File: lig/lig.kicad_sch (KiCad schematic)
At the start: 58 parts, among them J1 In_Smart, J10 OutSmart, J11 Conn_01x01_Female, J12 Conn_01x01_Female, J13 Conn_01x01_Female, J14 Conn_01x01_Female, J15 Conn_01x02_Male, J16 Conn_01x02_Socket, J2 OutSmart, J3 In_Dumb, J4 Out_Dumb, J5 OutSmart, J6 OutSmart, J7 OutSmart, J8 OutSmart, J9 OutSmart, U1 AP63205WU, U3 WeMos_D1_mini

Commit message: added footprint
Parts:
- added C5: 100pf only for 63200, Capacitor_SMD:C_0603_1608Metric, symbol Device:C
- added D27: LevelShifter Diode, Diode_SMD:D_SOD-123F, symbol Device:D
- added D31: Level Shifter Diode, Diode_SMD:D_SOD-123F, symbol Device:D
- added J17, J18: Conn_01x03, Connector_PinHeader_2.54mm:PinHeader_1x03_P2.54mm_Vertical, symbol Connector_Generic:Conn_01x03
- added JP1, JP2: Close, Resistor_SMD:R_0603_1608Metric_Pad0.98x0.95mm_HandSolder, symbol Jumper:SolderJumper_2_Open
- added JP4: close if using 4.5V (ap63200) or using diode shif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, Resistor_SMD:R_0603_1608Metric_Pad0.98x0.95mm_HandSolder, symbol Jumper:SolderJumper_2_Open
- added JP5: close for 63205, Resistor_SMD:R_0603_1608Metric_Pad0.98x0.95mm_HandSolder, symbol Jumper:SolderJumper_2_Open
- added Q1: 2N7000, Package_TO_SOT_SMD:SOT-23, symbol Transistor_FET:2N7000
- added R10, R11, R4, R5, R8, R9: 10k, Resistor_SMD:R_0603_1608Metric, symbol Device:R
- added R6: 30k only for 63200, Resistor_SMD:R_0603_1608Metric, symbol Device:R
- added R7: 140k only for 63200, Resistor_SMD:R_0603_1608Metric, symbol Device:R
- added U2: LM393, Package_SO:SOIC-8_3.9x4.9mm_P1.27mm, symbol Comparator:LM393
- J11, J12, J13, J14: symbol Connector:Conn_01x01_Female -> Connector:Conn_01x01_Socket
- J15: symbol Connector:Conn_01x02_Male -> Connector:Conn_01x02_Pin
- U1: value AP63205WU -> AP63205WU or AP63200
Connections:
- net 5V: now also C5.2, D27.2 (A), J17.3 (Pin_3), J18.3 (Pin_3), JP1.2 (B), JP5.2 (B), R11.1, R5.1, R6.1, U2.8 (V+); no longer D1.1 (VDD), U1.1 (FB)
- net GND: now also J17.1 (Pin_1), J18.1 (Pin_1), R7.2, R9.2, U2.4 (V-)
- net LDumbOut: now also J18.2 (Pin_2)
- net LOut: now also JP4.2 (B), Q1.3 (D), R11.2, R5.2, U2.1; no longer ESP1.30 (IO09), U3.11 (D4)
- net at D1.4 (DIN), R1.2, R2.2: now also J17.2 (Pin_2)
- net 3V3: now reaches U3.8 (3V3)
- net 3V3: now also ESP1.18 (3.3V), Q1.2 (G), R4.1, R8.1
- new net: D1.1 (VDD), D31.1 (K), JP2.1 (A)
- new net: D27.1 (K), D31.2 (A), JP1.1 (A), JP2.2 (B)
- new net: C5.1, JP5.1 (A), R6.2, R7.1, U1.1 (FB)
- new net: R10.2, U2.2 (-)
- new net: R8.2, R9.1, U2.3 (+)
- new net LOut3V3: ESP1.30 (IO09), JP4.1 (A), Q1.1 (S), R10.1, R4.2, U3.11 (D4)
- no-connect marks 18 -> 54
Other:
- moved on the sheet: C3, C4, J16

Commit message: v2 changes
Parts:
- removed R2: 1k, Resistor_SMD:R_0603_1608Metric, symbol Device:R
- added D32: 1A 5uA@1kV, Diode_SMD:D_SOD-123F, symbol Device:D
- D27, D31: LCSC C64898 -> (none)
- JP1, JP2, JP4, JP5: footprint Resistor_SMD:R_0603_1608Metric_Pad0.98x0.95mm_HandSolder -> Jumper:SolderJumper-2_P1.3mm_Bridged_Pad1.0x1.5mm
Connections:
- net 5V: now also D32.1 (K); no longer C3.1, C4.1, C5.2, J16.2 (Pin_2), JP5.2 (B), L1.2, R6.1
- net LOut: now also D1.4 (DIN), J17.2 (Pin_2), R1.2
- new net: C3.1, C4.1, C5.2, D32.2 (A), J16.2 (Pin_2), JP5.2 (B), L1.2, R6.1
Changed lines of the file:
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@@
   (junction (at 203.835 156.21) (diameter 0) (color 0 0 0 0)
   )
+  (junction (at 156.21 167.005) (diameter 0) (color 0 0 0 0)
+  )
   (junction (at 175.26 86.995) (diameter 0) (color 0 0 0 0)
   )
@@
     (stroke (width 0) (type default))
   )
+  (wire (pts (xy 165.1 26.67) (xy 172.72 26.67))
+    (stroke (width 0) (type default))
+  )
   (wire (pts (xy 33.02 132.08) (xy 33.02 146.685))
     (stroke (width 0) (type default))
@@
     )
   )
-  (global_label "5V" (shape input) (at 156.21 167.005 0) (fields_autoplaced)
+  (global_label "5V" (shape input) (at 163.83 167.005 0) (fields_autoplaced)
     (effects (font (size 1.27 1.27)) (justify left))
-    (property "Intersheetrefs" "${INTERSHEET_REFS}" (at 160.9212 166.9256 0)
+    (property "Intersheetrefs" "${INTERSHEET_REFS}" (at 168.5412 166.9256 0)
       (effects (font (size 1.27 1.27)) (justify left) hide)
     )
@@
       (effects (font (size 1.27 1.27)))
     )
-    (property "Footprint" "Resistor_SMD:R_0603_1608Metric_Pad0.98x0.95mm_HandSolder" (at 192.405 16.51 0)
+    (property "Footprint" "Jumper:SolderJumper-2_P1.3mm_Bridged_Pad1.0x1.5mm" (at 192.405 16.51 0)
       (effects (font (size 1.27 1.27)) hide)
     )
@@
       (effects (font (size 1.27 1.27)) (justify right))
     )
-    (property "Footprint" "Resistor_SMD:R_0603_1608Metric_Pad0.98x0.95mm_HandSolder" (at 125.73 170.815 0)
+    (property "Footprint" "Jumper:SolderJumper-2_P1.3mm_Bridged_Pad1.0x1.5mm" (at 125.73 170.815 0)
       (effects (font (size 1.27 1.27)) hide)
     )
@@
       (effects (font (size 1.27 1.27)))
     )
-    (property "Footprint" "Resistor_SMD:R_0603_1608Metric_Pad0.98x0.95mm_HandSolder" (at 203.835 127 0)
+    (property "Footprint" "Jumper:SolderJumper-2_P1.3mm_Bridged_Pad1.0x1.5mm" (at 203.835 127 0)
       (effects (font (size 1.27 1.27)) hide)
     )
@@
       (effects (font (size 1.27 1.27)) hide)
     )
-    (property "LCSC" "C64898" (at 192.405 12.7 0)
+    (property "LCSC" "" (at 192.405 12.7 0)
       (effects (font (size 1.27 1.27)) hide)
     )
@@
       (effects (font (size 1.27 1.27)))
     )
-    (property "Footprint" "Resistor_SMD:R_0603_1608Metric_Pad0.98x0.95mm_HandSolder" (at 201.295 16.51 0)
+    (property "Footprint" "Jumper:SolderJumper-2_P1.3mm_Bridged_Pad1.0x1.5mm" (at 201.295 16.51 0)
       (effects (font (size 1.27 1.27)) hide)
     )
@@
     )
   )
-  (symbol (lib_id "Device:R") (at 168.91 26.67 90) (unit 1)
-    (in_bom yes) (on_board yes) (dnp no) (fields_autoplaced)
-    (property "Reference" "R2" (at 168.91 20.32 90)
-      (effects (font (size 1.27 1.27)))
-    )
-    (property "Value" "1k" (at 168.91 22.86 90)
-      (effects (font (size 1.27 1.27)))
-    )
-    (property "Footprint" "Resistor_SMD:R_0603_1608Metric" (at 168.91 28.448 90)
-      (effects (font (size 1.27 1.27)) hide)
-    )
-    (property "Datasheet" "~" (at 168.91 26.67 0)
-      (effects (font (size 1.27 1.27)) hide)
-    )
-    (property "LCSC" "C21190" (at 168.91 26.67 0)
-      (effects (font (size 1.27 1.27)) hide)
-    )
-    (pin "1")
-    (pin "2")
-    (instances
-      (project "lig"
-        (path "/03d6a00f-a8c8-4eb8-91ea-299864b30e8f"
-          (reference "R2") (unit 1)
-        )
-      )
-    )
-  )
   (symbol (lib_id "Device:C") (at 138.43 175.895 0) (unit 1)
     (in_bom yes) (on_board yes) (dnp no) (fields_autoplaced)
@@
       (effects (font (size 1.27 1.27)) hide)
     )
-    (property "LCSC" "C64898" (at 201.295 12.7 0)
+    (property "LCSC" "" (at 201.295 12.7 0)
       (effects (font (size 1.27 1.27)) hide)
     )
@@
         )
       )
+    )
+  )
+  (symbol (lib_id "Device:D") (at 160.02 167.005 180) (unit 1)
+    (in_bom yes) (on_board yes) (dnp no) (fields_autoplaced)
+    (property "Reference" "D32" (at 160.02 160.02 0)
+      (effects (font (size 1.27 1.27)))
+    )
+    (property "Value" "1A 5uA@1kV" (at 160.02 162.56 0)
+      (effects (font (size 1.27 1.27)))
+    )
+    (property "Footprint" "Diode_SMD:D_SOD-123F" (at 160.02 167.005 0)
+      (effects (font (size 1.27 1.27)) hide)
+    )
+    (property "Datasheet" "~" (at 160.02 167.005 0)
+      (effects (font (size 1.27 1.27)) hide)
+    )
+    (property "LCSC" "C64898" (at 160.02 167.005 0)
+      (effects (font (size 1.27 1.27)) hide)
+    )
+    (property "Sim.Device" "D" (at 160.02 167.005 0)
+      (effects (font (size 1.27 1.27)) hide)
+    )
+    (property "Sim.Pins" "1=K 2=A" (at 160.02 167.005 0)
+      (effects (font (size 1.27 1.27)) hide)
+    )
+    (pin "1")
+    (pin "2")
+    (instances
+      (project "lig"
+        (path "/03d6a00f-a8c8-4eb8-91ea-299864b30e8f"
+          (reference "D32") (unit 1)
+        )
+      )

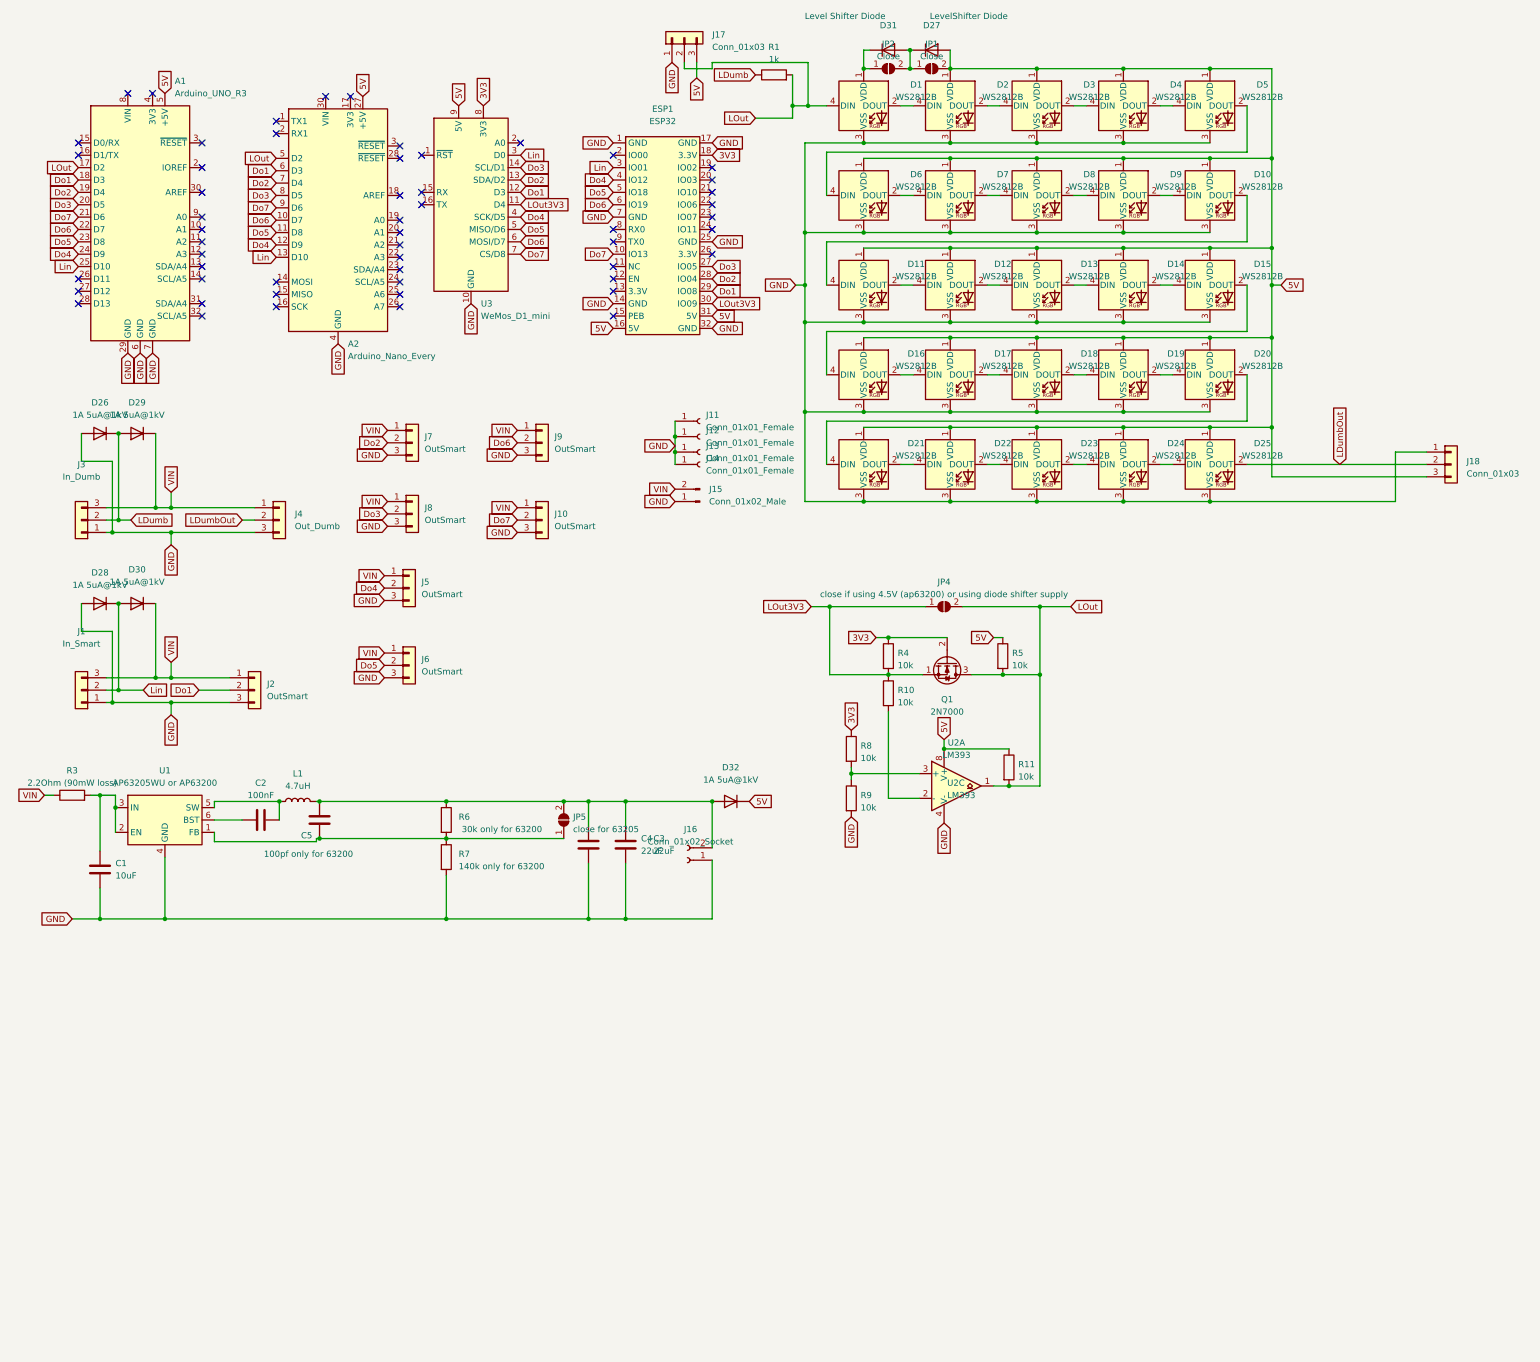
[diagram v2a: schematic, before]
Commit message: v2 diodes and simplification
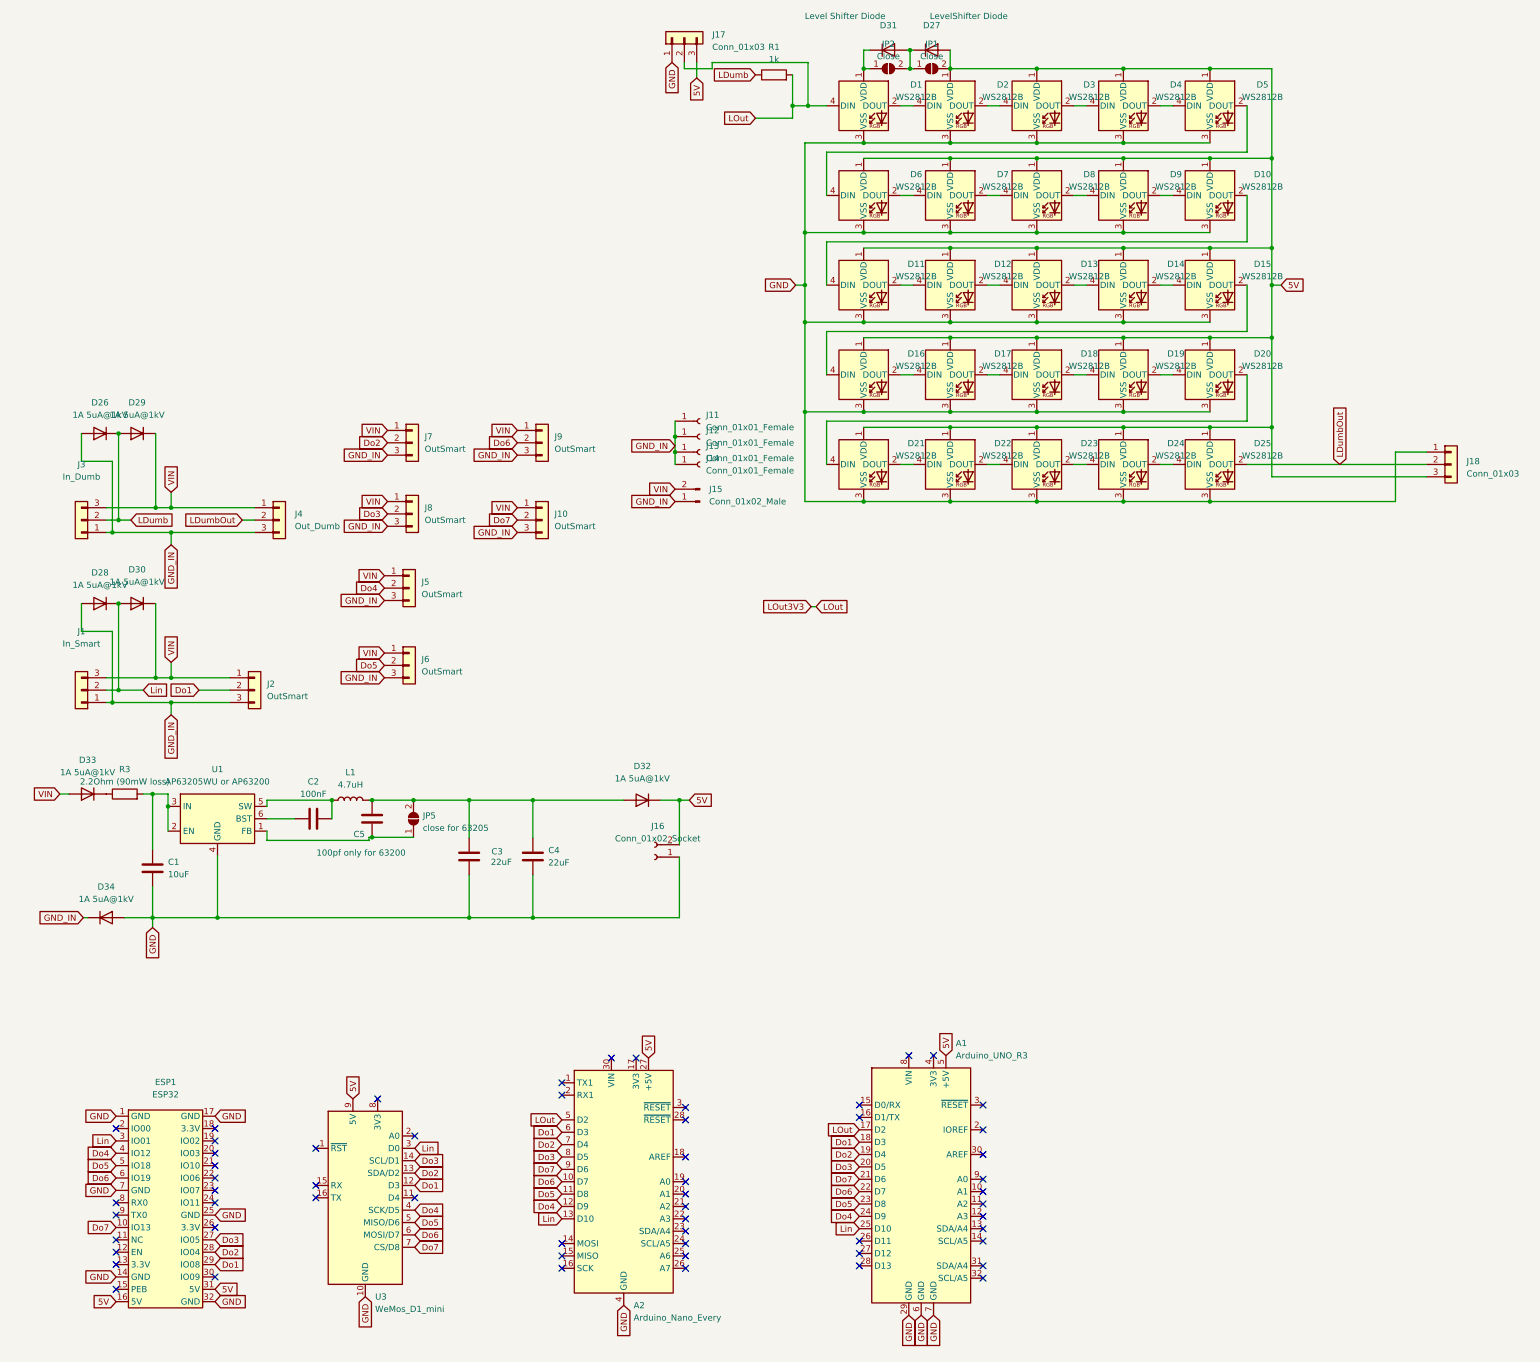
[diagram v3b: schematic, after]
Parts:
- removed JP4: close if using 4.5V (ap63200) or using diode shif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, Jumper:SolderJumper-2_P1.3mm_Bridged_Pad1.0x1.5mm, symbol Jumper:SolderJumper_2_Open
- removed Q1: 2N7000, Package_TO_SOT_SMD:SOT-23, symbol Transistor_FET:2N7000
- removed R10, R11, R4, R5, R8, R9: 10k, Resistor_SMD:R_0603_1608Metric, symbol Device:R
- removed R6: 30k only for 63200, Resistor_SMD:R_0603_1608Metric, symbol Device:R
- removed R7: 140k only for 63200, Resistor_SMD:R_0603_1608Metric, symbol Device:R
- removed U2: LM393, Package_SO:SOIC-8_3.9x4.9mm_P1.27mm, symbol Comparator:LM393
- added D33, D34: 1A 5uA@1kV, Diode_SMD:D_SOD-123F, symbol Device:D
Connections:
- net 5V: now also J16.2 (Pin_2)
- net GND: now also D34.2 (A); no longer D26.2 (A), D28.2 (A), J1.1 (Pin_1), J10.3 (Pin_3), J11.1 (Pin_1), J12.1 (Pin_1), J13.1 (Pin_1), J14.1 (Pin_1), J15.1 (Pin_1), J2.3 (Pin_3), J3.1 (Pin_1), J4.3 (Pin_3), J5.3 (Pin_3), J6.3 (Pin_3), J7.3 (Pin_3), J8.3 (Pin_3), J9.3 (Pin_3)
- net VIN: now also D33.2 (A); no longer R3.1
- net at C3.1, C4.1, C5.2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: no longer J16.2 (Pin_2)
- net 3V3: no longer names the net of U3.8 (3V3)
- net 3V3: no longer ESP1.18 (3.3V)
- net LOut3V3: no longer names the net of U3.11 (D4)
- net LOut3V3: no longer ESP1.30 (IO09)
- new net: D33.1 (K), R3.1
- new net GND_IN: D26.2 (A), D28.2 (A), D34.1 (K), J1.1 (Pin_1), J10.3 (Pin_3), J11.1 (Pin_1), J12.1 (Pin_1), J13.1 (Pin_1), J14.1 (Pin_1), J15.1 (Pin_1), J2.3 (Pin_3), J3.1 (Pin_1), J4.3 (Pin_3), J5.3 (Pin_3), J6.3 (Pin_3), J7.3 (Pin_3), J8.3 (Pin_3), J9.3 (Pin_3)
- no-connect marks 54 -> 58
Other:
- moved on the sheet: A1, A2, C1, C2, C3, C4, C5, D32, ESP1, J16, JP5, L1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
